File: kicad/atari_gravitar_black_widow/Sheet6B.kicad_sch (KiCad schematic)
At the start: 20 parts

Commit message: placements
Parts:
- L_4, M_4, N_5, R_4: footprint (none) -> Star_Wars_Vector_PCB:DIP14
- N_3, N_4, P_4, R_3: footprint (none) -> Star_Wars_Vector_PCB:DIP16
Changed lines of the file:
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@@
     (property "Reference" "R_4" (id 0) (at 399.415 95.885 0))
     (property "Value" "LS32" (id 1) (at 399.415 98.425 0))
-    (property "Footprint" "" (id 2) (at 399.415 97.155 0)
+    (property "Footprint" "Star_Wars_Vector_PCB:DIP14" (id 2) (at 399.415 97.155 0)
       (effects (font (size 1.27 1.27)) hide)
     )
@@
     (property "Reference" "L_4" (id 0) (at 421.005 217.17 0))
     (property "Value" "LS08" (id 1) (at 421.005 219.71 0))
-    (property "Footprint" "" (id 2) (at 421.005 218.44 0)
+    (property "Footprint" "Star_Wars_Vector_PCB:DIP14" (id 2) (at 421.005 218.44 0)
       (effects (font (size 1.27 1.27)) hide)
     )
@@
     (property "Reference" "M_4" (id 0) (at 151.13 170.18 0))
     (property "Value" "LS27" (id 1) (at 151.003 174.498 0))
-    (property "Footprint" "" (id 2) (at 151.13 171.45 0)
+    (property "Footprint" "Star_Wars_Vector_PCB:DIP14" (id 2) (at 151.13 171.45 0)
       (effects (font (size 1.27 1.27)) hide)
     )
@@
     (property "Reference" "R_4" (id 0) (at 323.85 255.905 0))
     (property "Value" "LS32" (id 1) (at 323.85 258.445 0))
-    (property "Footprint" "" (id 2) (at 323.85 257.175 0)
+    (property "Footprint" "Star_Wars_Vector_PCB:DIP14" (id 2) (at 323.85 257.175 0)
       (effects (font (size 1.27 1.27)) hide)
     )
@@
     (property "Reference" "N_5" (id 0) (at 248.92 274.32 0))
     (property "Value" "LS02" (id 1) (at 248.92 276.86 0))
-    (property "Footprint" "" (id 2) (at 248.92 275.59 0)
+    (property "Footprint" "Star_Wars_Vector_PCB:DIP14" (id 2) (at 248.92 275.59 0)
       (effects (font (size 1.27 1.27)) hide)
     )
@@
     (property "Reference" "N_3" (id 0) (at 283.21 288.925 0))
     (property "Value" "LS157A" (id 1) (at 283.845 292.1 0))
-    (property "Footprint" "" (id 2) (at 283.21 290.83 0)
+    (property "Footprint" "Star_Wars_Vector_PCB:DIP16" (id 2) (at 283.21 290.83 0)
       (effects (font (size 1.27 1.27)) hide)
     )
@@
     (property "Reference" "R_3" (id 0) (at 283.21 344.805 0))
     (property "Value" "LS157B" (id 1) (at 283.21 347.345 0))
-    (property "Footprint" "" (id 2) (at 283.21 346.075 0)
+    (property "Footprint" "Star_Wars_Vector_PCB:DIP16" (id 2) (at 283.21 346.075 0)
       (effects (font (size 1.27 1.27)) hide)
     )
@@
     (property "Reference" "N_4" (id 0) (at 336.55 288.29 0))
     (property "Value" "S129" (id 1) (at 336.55 290.195 0))
-    (property "Footprint" "" (id 2) (at 336.55 289.56 0)
+    (property "Footprint" "Star_Wars_Vector_PCB:DIP16" (id 2) (at 336.55 289.56 0)
       (effects (font (size 1.27 1.27)) hide)
     )
@@
     (property "Reference" "P_4" (id 0) (at 389.89 285.75 0))
     (property "Value" "LS174A" (id 1) (at 389.89 288.29 0))
-    (property "Footprint" "" (id 2) (at 389.89 287.02 0)
-      (effects (font (size 1.27 1.27)) hide)
-    )
+    (property "Footprint" "Star_Wars_Vector_PCB:DIP16" (id 2) (at 389.89 287.02 0)
+      (effects (font (size 1.27 1.27)) hide)
+    )

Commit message: TEST POINTS PLACED
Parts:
- TPSACLK1, TP~SA1: footprint (none) -> quantum_arcade_pcb:TP
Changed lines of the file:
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@@
       (effects (font (size 1.524 1.524)) hide)
     )
-    (property "Footprint" "" (id 2) (at 353.06 92.075 0)
+    (property "Footprint" "quantum_arcade_pcb:TP" (id 2) (at 353.06 92.075 0)
       (effects (font (size 1.524 1.524)) hide)
     )
@@
       (effects (font (size 1.524 1.524)) hide)
     )
-    (property "Footprint" "" (id 2) (at 272.415 186.055 0)
+    (property "Footprint" "quantum_arcade_pcb:TP" (id 2) (at 272.415 186.055 0)
       (effects (font (size 1.524 1.524)) hide)
     )

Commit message: resistor placements R1-R153
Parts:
- R20: footprint (none) -> Star_Wars_Vector_PCB:GenericComp
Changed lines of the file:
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@@
     (property "Reference" "R20" (id 0) (at 371.475 88.9 90))
     (property "Value" "10K" (id 1) (at 371.475 85.09 90))
-    (property "Footprint" "" (id 2) (at 371.221 88.011 90)
+    (property "Footprint" "Star_Wars_Vector_PCB:GenericComp" (id 2) (at 371.221 88.011 90)
       (effects (font (size 1.27 1.27)) hide)
     )

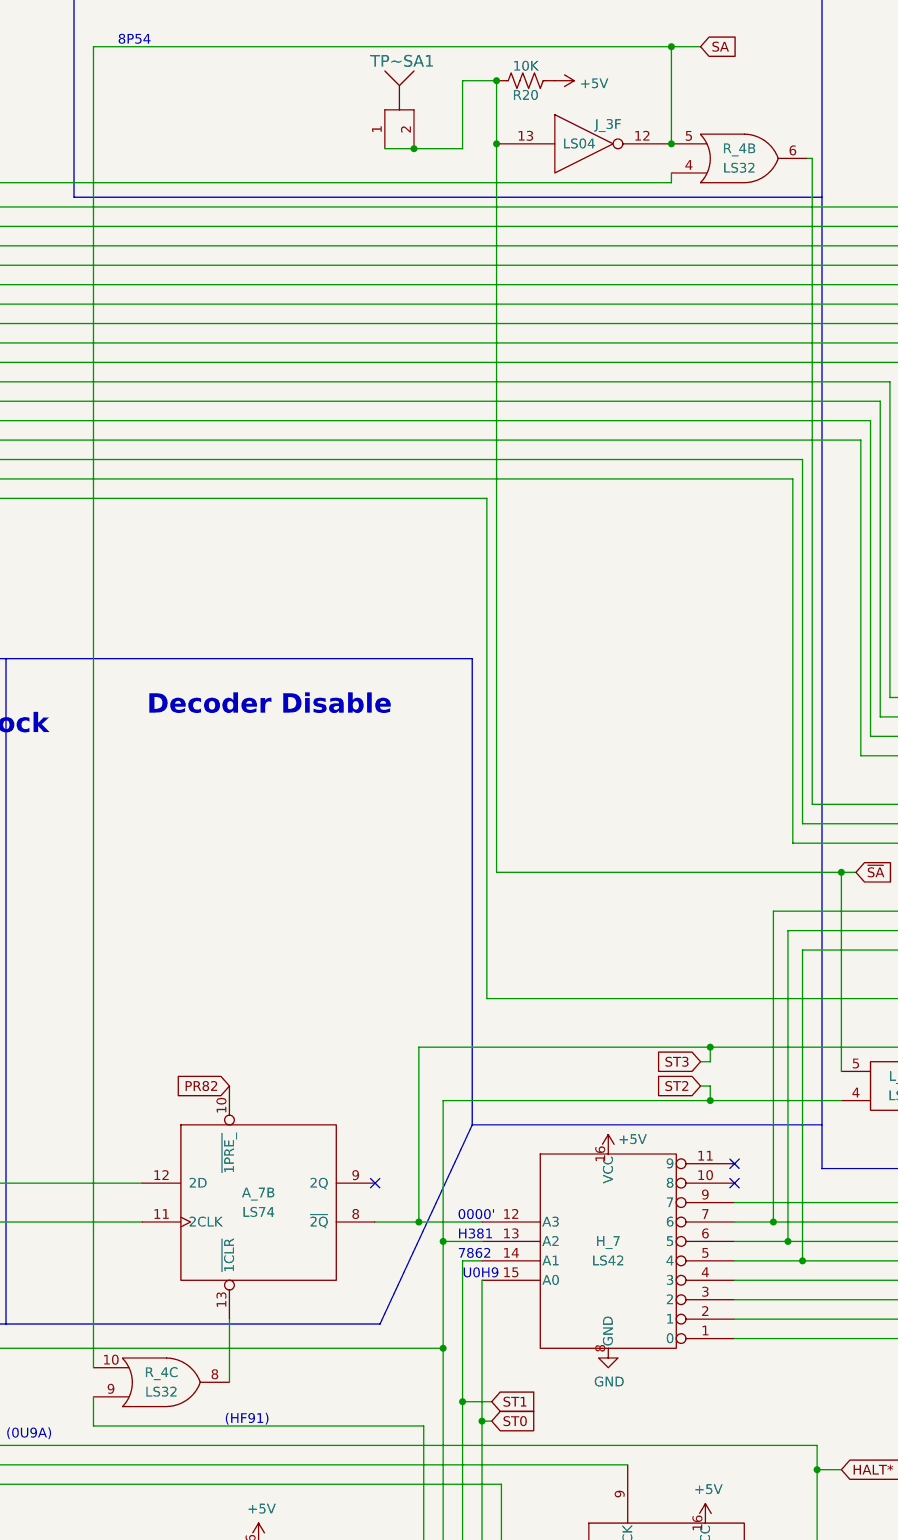
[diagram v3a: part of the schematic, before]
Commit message: Fixed all schematic warnings and fixed the edge cuts
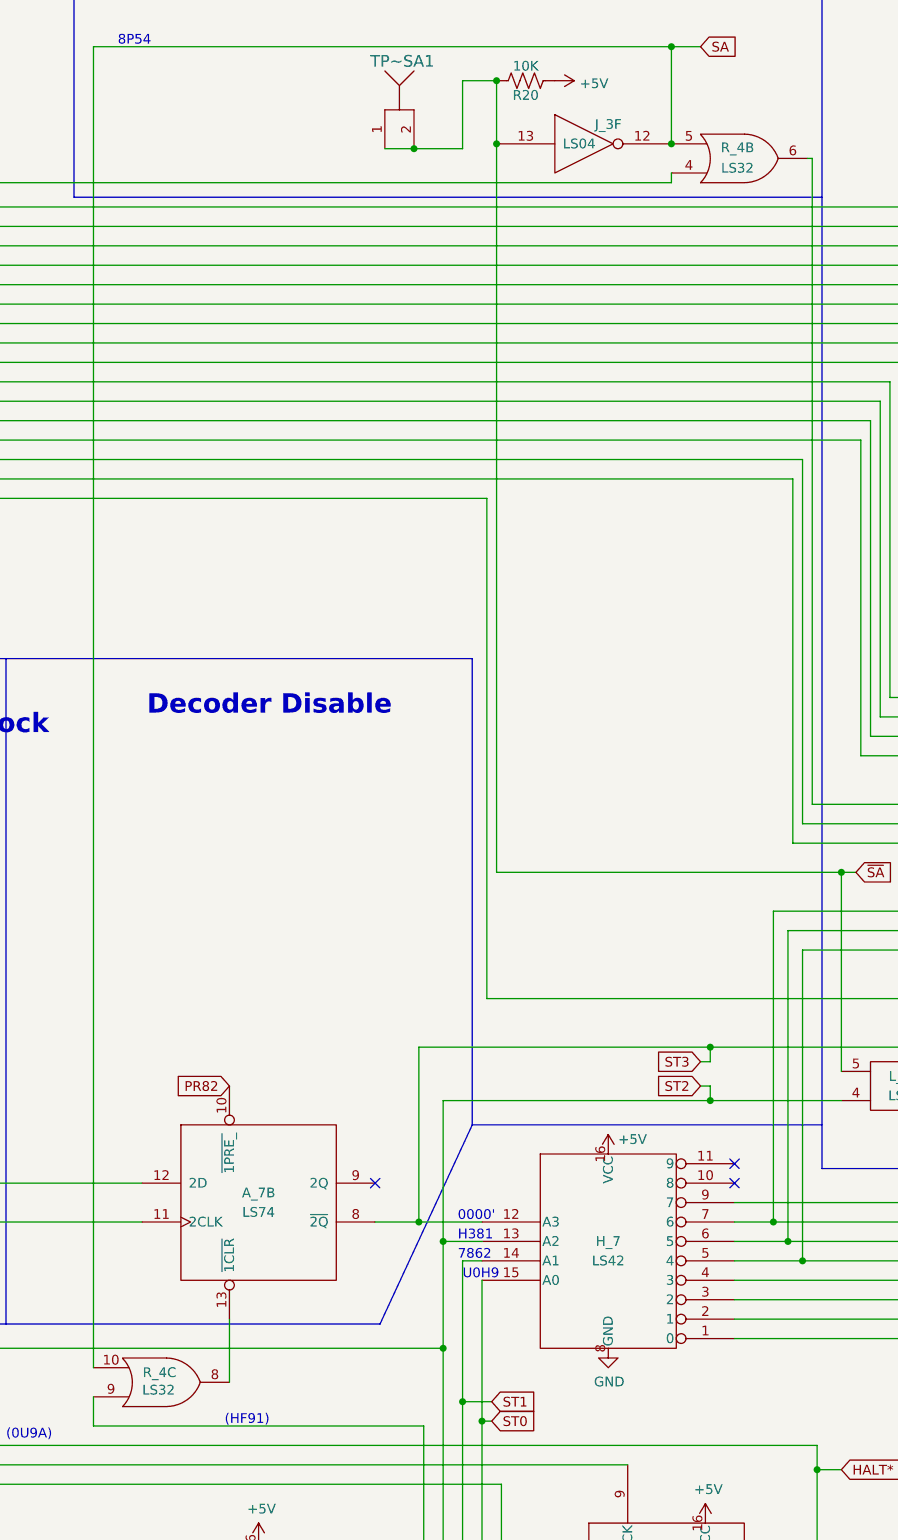
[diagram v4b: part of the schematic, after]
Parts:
- removed R_4: LS32, Star_Wars_Vector_PCB:DIP14, symbol atari_grav_bw:LS32
- added R_4: LS32, Star_Wars_Vector_PCB:DIP14, symbol Star_Wars_Vector_PCB:LS32
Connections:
- net SA: now also R_4.10, R_4.5
- net ~{OP2}: now also R_4.4
- net at J_9.5 (~{OP2}): now also R_4.6
- net at A_7.13 (~{1CLR}): now also R_4.8
- net at N_4.9 (O4), P_4.6 (3D): now also R_4.9
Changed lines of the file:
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@@
   (junction (at 358.14 285.75) (diameter 0) (color 0 0 0 0)
   )
+  (junction (at 390.525 95.25) (diameter 0) (color 0 0 0 0)
+  )
   (junction (at 367.665 86.995) (diameter 0) (color 0 0 0 0)
   )
@@
   )
   (junction (at 73.025 196.215) (diameter 0) (color 0 0 0 0)
-  )
-  (junction (at 390.525 95.25) (diameter 0) (color 0 0 0 0)
   )
   (junction (at 267.335 211.455) (diameter 0) (color 0 0 0 0)
@@
     (pin "12")
     (pin "13")
-  )
-  (symbol (lib_id "atari_grav_bw:LS32") (at 399.415 97.155 0) (mirror x) (unit 2)
-    (in_bom yes) (on_board yes)
-    (property "Reference" "R_4" (id 0) (at 399.415 95.885 0))
-    (property "Value" "LS32" (id 1) (at 399.415 98.425 0))
-    (property "Footprint" "Star_Wars_Vector_PCB:DIP14" (id 2) (at 399.415 97.155 0)
-      (effects (font (size 1.27 1.27)) hide)
-    )
-    (property "Datasheet" "" (id 3) (at 399.415 97.155 0)
-      (effects (font (size 1.27 1.27)) hide)
-    )
-    (pin "4")
-    (pin "5")
-    (pin "6")
   )
   (symbol (lib_id "atari_grav_bw:AVG") (at 449.58 177.8 0) (unit 1)
@@
     (pin "1")
   )
-  (symbol (lib_id "atari_grav_bw:LS32") (at 323.85 257.175 0) (mirror x) (unit 3)
-    (in_bom yes) (on_board yes)
-    (property "Reference" "R_4" (id 0) (at 323.85 255.905 0))
-    (property "Value" "LS32" (id 1) (at 323.85 258.445 0))
-    (property "Footprint" "Star_Wars_Vector_PCB:DIP14" (id 2) (at 323.85 257.175 0)
-      (effects (font (size 1.27 1.27)) hide)
-    )
-    (property "Datasheet" "" (id 3) (at 323.85 257.175 0)
-      (effects (font (size 1.27 1.27)) hide)
-    )
-    (pin "10")
-    (pin "8")
-    (pin "9")
-  )
   (symbol (lib_id "atari_grav_bw:LS02") (at 248.92 275.59 0) (unit 3)
     (in_bom yes) (on_board yes)
@@
     (pin "1")
   )
+  (symbol (lib_id "Star_Wars_Vector_PCB:LS32") (at 323.85 257.175 0) (mirror x) (unit 3)
+    (in_bom yes) (on_board yes)
+    (property "Reference" "R_4" (id 0) (at 323.596 255.905 0))
+    (property "Value" "LS32" (id 1) (at 323.469 258.191 0))
+    (property "Footprint" "Star_Wars_Vector_PCB:DIP14" (id 2) (at 323.85 257.175 0)
+      (effects (font (size 1.27 1.27)) hide)
+    )
+    (property "Datasheet" "" (id 3) (at 323.85 257.175 0)
+      (effects (font (size 1.27 1.27)) hide)
+    )
+    (pin "10")
+    (pin "8")
+    (pin "9")
+  )
+  (symbol (lib_id "Star_Wars_Vector_PCB:LS32") (at 399.415 97.155 0) (mirror x) (unit 2)
+    (in_bom yes) (on_board yes)
+    (property "Reference" "R_4" (id 0) (at 399.161 95.758 0))
+    (property "Value" "LS32" (id 1) (at 399.161 98.425 0))
+    (property "Footprint" "Star_Wars_Vector_PCB:DIP14" (id 2) (at 399.415 97.155 0)
+      (effects (font (size 1.27 1.27)) hide)
+    )
+    (property "Datasheet" "" (id 3) (at 399.415 97.155 0)
+      (effects (font (size 1.27 1.27)) hide)
+    )
+    (pin "4")
+    (pin "5")
+    (pin "6")
+  )
   (symbol (lib_id "power:GND") (at 292.1 224.155 0) (unit 1)

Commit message: Row 3 - 3.5 tracess
Also fixed some schematic errors (IO at J6, power at R4, Z out TP)
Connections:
- net AM0: now also R_3.3 (B); no longer R_3.2 (A)
- net F0: now also R_3.2 (A); no longer R_3.3 (B)

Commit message: lots o' traces
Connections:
- net ST2: now also M_4.11; no longer M_4.10
- net ~{VMEM}: now also M_4.9; no longer M_4.11
- net at K_3.9 (2Q), K_5.3: now also M_4.10; no longer M_4.9
- net at R_3.4 (Y): now also N_4.5 (A0); no longer N_4.7 (A2)
- net at R_3.9 (Y): now also N_4.7 (A2); no longer N_4.5 (A0)
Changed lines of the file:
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@@
   (junction (at 365.76 262.255) (diameter 0) (color 0 0 0 0)
   )
-  (junction (at 74.93 175.26) (diameter 0) (color 0 0 0 0)
-  )
   (junction (at 206.375 217.805) (diameter 0) (color 0 0 0 0)
+  )
+  (junction (at 74.93 171.4754) (diameter 0) (color 0 0 0 0)
   )
   (junction (at 407.67 360.045) (diameter 0) (color 0 0 0 0)
@@
     (stroke (width 0) (type default) (color 0 0 0 0))
   )
+  (wire (pts (xy 74.93 171.4754) (xy 74.93 252.73))
+    (stroke (width 0) (type default) (color 0 0 0 0))
+  )
   (wire (pts (xy 363.22 86.995) (xy 367.665 86.995))
     (stroke (width 0) (type default) (color 0 0 0 0))
@@
     (stroke (width 0) (type default) (color 0 0 0 0))
   )
-  (wire (pts (xy 67.31 175.26) (xy 74.93 175.26))
-    (stroke (width 0) (type default) (color 0 0 0 0))
-  )
   (wire (pts (xy 196.215 191.77) (xy 166.37 179.705))
     (stroke (width 0) (type default) (color 0 0 0 0))
@@
     (stroke (width 0) (type default) (color 0 0 0 0))
   )
+  (wire (pts (xy 134.5438 171.4754) (xy 137.16 171.45))
+    (stroke (width 0) (type default) (color 0 0 0 0))
+  )
   (wire (pts (xy 416.56 172.72) (xy 430.53 172.72))
     (stroke (width 0) (type default) (color 0 0 0 0))
@@
     (stroke (width 0) (type default) (color 0 0 0 0))
   )
+  (wire (pts (xy 74.93 171.4754) (xy 134.5438 171.4754))
+    (stroke (width 0) (type default) (color 0 0 0 0))
+  )
   (wire (pts (xy 312.42 342.265) (xy 302.26 342.265))
     (stroke (width 0) (type default) (color 0 0 0 0))
@@
     (stroke (width 0) (type default) (color 0 0 0 0))
   )
-  (wire (pts (xy 74.93 252.73) (xy 74.93 175.26))
-    (stroke (width 0) (type default) (color 0 0 0 0))
-  )
   (wire (pts (xy 264.16 337.185) (xy 67.31 337.185))
     (stroke (width 0) (type default) (color 0 0 0 0))
@@
     (stroke (width 0) (type default) (color 0 0 0 0))
   )
-  (wire (pts (xy 74.93 175.26) (xy 134.62 175.26))
+  (wire (pts (xy 67.2338 171.4754) (xy 74.93 171.4754))
     (stroke (width 0) (type default) (color 0 0 0 0))
   )
@@
     (stroke (width 0) (type default) (color 0 0 0 0))
   )
-  (wire (pts (xy 133.35 171.45) (xy 133.35 187.96))
+  (wire (pts (xy 134.62 175.26) (xy 134.6155 187.9583))
     (stroke (width 0) (type default) (color 0 0 0 0))
   )
@@
     (stroke (width 0) (type default) (color 0 0 0 0))
   )
-  (wire (pts (xy 133.35 171.45) (xy 137.16 171.45))
-    (stroke (width 0) (type default) (color 0 0 0 0))
-  )
   (wire (pts (xy 476.25 189.23) (xy 468.63 189.23))
     (stroke (width 0) (type default) (color 0 0 0 0))
@@
     (stroke (width 0) (type default) (color 0 0 0 0))
   )
-  (wire (pts (xy 133.35 187.96) (xy 141.605 187.96))
+  (wire (pts (xy 134.6155 187.9583) (xy 141.605 187.96))
     (stroke (width 0) (type default) (color 0 0 0 0))
   )
@@
     (effects (font (size 2.54 2.54) (thickness 0.508) bold) (justify left bottom))
   )
-  (text "(H381)" (at 68.58 175.26 0)
+  (text "(H381)" (at 68.326 171.0436 0)
     (effects (font (size 1.27 1.27)) (justify left bottom))
   )
@@
     )
   )
-  (global_label "ST2" (shape input) (at 67.31 175.26 180) (fields_autoplaced)
-    (effects (font (size 1.27 1.27)) (justify right))
-    (property "Intersheet References" "${INTERSHEET_REFS}" (id 0) (at 0 0 0)
+  (global_label "ST2" (shape input) (at 67.2338 171.4754 180) (fields_autoplaced)
+    (effects (font (size 1.27 1.27)) (justify right))
+    (property "Intersheet References" "${INTERSHEET_REFS}" (id 0) (at -0.0762 -3.7846 0)
       (effects (font (size 1.27 1.27)) hide)
     )
@@
   )
   (global_label "~{OP0}" (shape input) (at 67.31 139.065 180) (fields_autoplaced)
-    (effects (font (size 0.8382 0.8382)) (justify right))
-    (property "Intersheet References" "${INTERSHEET_REFS}" (id 0) (at 0 0 0)
-      (effects (font (size 1.27 1.27)) hide)
+    (effects (font (size 1.27 1.27)) (justify right))
+    (property "Intersheet References" "${INTERSHEET_REFS}" (id 0) (at 61.1758 138.9856 0)
+      (effects (font (size 1.27 1.27)) (justify right) hide)
     )
   )
@@
   )
   (global_label "~{VMEM}" (shape input) (at 67.31 167.64 180) (fields_autoplaced)
-    (effects (font (size 0.8382 0.8382)) (justify right))
-    (property "Intersheet References" "${INTERSHEET_REFS}" (id 0) (at 0 0 0)
-      (effects (font (size 1.27 1.27)) hide)
+    (effects (font (size 1.27 1.27)) (justify right))
+    (property "Intersheet References" "${INTERSHEET_REFS}" (id 0) (at 59.8453 167.5606 0)
+      (effects (font (size 1.27 1.27)) (justify right) hide)
     )
   )
@@
   )
   (global_label "~{VGGO}" (shape input) (at 67.31 141.605 180) (fields_autoplaced)
-    (effects (font (size 0.8382 0.8382)) (justify right))
-    (property "Intersheet References" "${INTERSHEET_REFS}" (id 0) (at 0 0 0)
-      (effects (font (size 1.27 1.27)) hide)
-    )
-  )
+    (effects (font (size 1.27 1.27)) (justify right))
+    (property "Intersheet References" "${INTERSHEET_REFS}" (id 0) (at 60.0268 141.5256 0)
+      (effects (font (size 1.27 1.27)) (justify right) hide)
+    )
+  )
